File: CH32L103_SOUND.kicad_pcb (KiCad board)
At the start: 2 copper layers, 38 x 19.6 mm, 47 parts, among them J1 USB_C_Receptacle_PowerOnly_6P, J2 Conn_01x04, J3 Conn_01x05, J4 Conn_01x02, Q1 AO3400A, U1 USBLC6-2SC6, U2 TP4057, U3 HT7533-1, U4 CS588, U5 CH32L103F8U6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

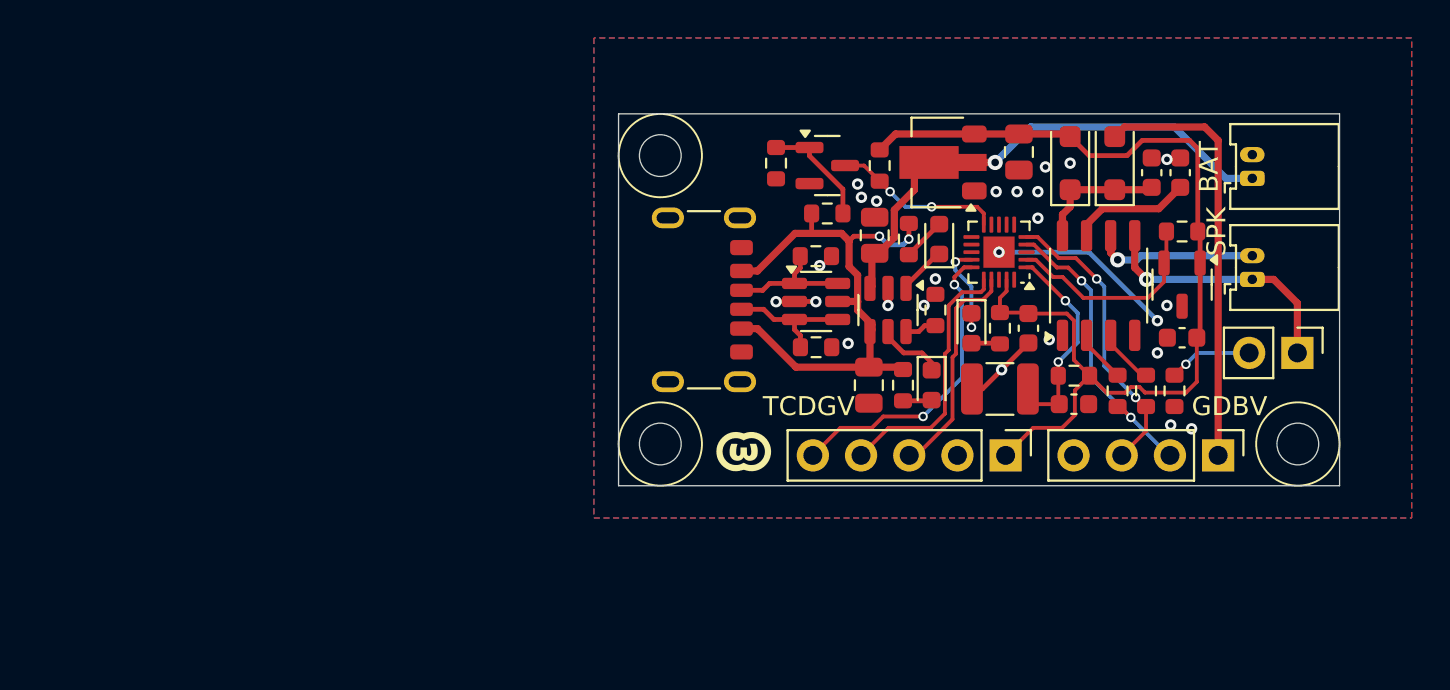
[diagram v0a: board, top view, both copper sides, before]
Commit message: 修改引脚布局
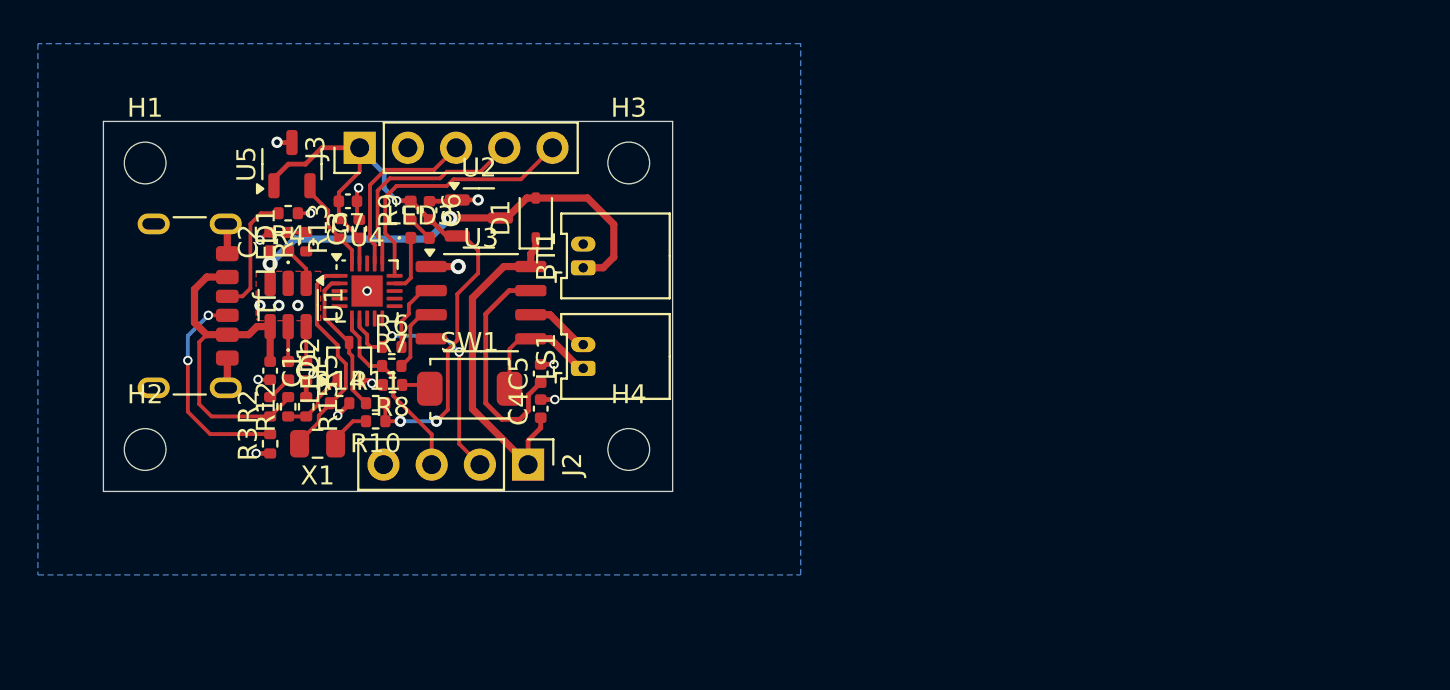
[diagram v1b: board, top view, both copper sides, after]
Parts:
- removed C8: 100NF, Capacitor_SMD:C_0603_1608Metric
- removed D2: K36, Diode_SMD:D_SOD-123F
- removed G***: LOGO, LOGO
- removed J4: Conn_01x02, Connector_PinHeader_2.54mm:PinHeader_1x02_P2.54mm_Vertical
- removed REF**: KiCad-Logo2_5mm_SilkScreen, Symbol:KiCad-Logo2_5mm_SilkScreen
- removed REF**: OSHW-Symbol_6.7x6mm_SilkScreen, Symbol:OSHW-Symbol_6.7x6mm_SilkScreen
- removed U6: CC6201, Package_TO_SOT_SMD:SOT-23-3
- added H4: MountingHole, MountingHole:MountingHole_2.2mm_M2_ISO14580, F.Cu at (83.4, 64.0)
- added R15: 10K, Resistor_SMD:R_0402_1005Metric, F.Cu at (66.4, 61.7)
- added SW1: SW_Push, Maiooo_Library:Button_2P, F.Cu at (75.0, 60.8)
- C1, C2, C3: footprint Capacitor_SMD:C_0805_2012Metric -> Capacitor_SMD:C_0402_1005Metric
- C4, C5, C6: footprint Capacitor_SMD:C_0603_1608Metric -> Capacitor_SMD:C_0402_1005Metric
- C7: value 50PF -> 100NF; footprint Capacitor_SMD:C_0603_1608Metric -> Capacitor_SMD:C_0402_1005Metric
- D1: value K36 -> 1N5819WS; footprint Diode_SMD:D_SOD-123F -> Diode_SMD:D_SOD-323
- LED1, LED2, LED3: footprint LED_SMD:LED_0603_1608Metric -> LED_SMD:LED_0402_1005Metric
- Q1: value AO3400A -> 2N7002W; footprint Package_TO_SOT_SMD:SOT-23 -> Package_TO_SOT_SMD:SOT-323_SC-70
- R1, R2, R3, R4, R5, R6, R7, R8, R9: footprint Resistor_SMD:R_0603_1608Metric -> Resistor_SMD:R_0402_1005Metric
- R10, R12: value 100K -> 1K; footprint Resistor_SMD:R_0603_1608Metric -> Resistor_SMD:R_0402_1005Metric
- R11: value 1K -> 1M; footprint Resistor_SMD:R_0603_1608Metric -> Resistor_SMD:R_0402_1005Metric
- R13: value 100K -> 1M; footprint Resistor_SMD:R_0603_1608Metric -> Resistor_SMD:R_0402_1005Metric
- R14: value 10K -> 1M; footprint Resistor_SMD:R_0603_1608Metric -> Resistor_SMD:R_0402_1005Metric
- U1: value USBLC6-2SC6 -> TP4057; footprint Package_TO_SOT_SMD:SOT-23-6 -> Package_TO_SOT_SMD:TSOT-23-6
- U2: value TP4057 -> HT7533-1; footprint Package_TO_SOT_SMD:TSOT-23-6 -> Maiooo_Library:HT7533s
- U3: value HT7533-1 -> CS588; footprint Package_TO_SOT_SMD:SOT-89-3 -> Package_SO:SOP-8_3.9x4.9mm_P1.27mm
- U4: value CS588 -> CH32L103F8U6; footprint Package_SO:SOP-8_3.9x4.9mm_P1.27mm -> Package_DFN_QFN:QFN-20-1EP_3x3mm_P0.4mm_EP1.65x1.65mm
- U5: value CH32L103F8U6 -> CC6201; footprint Package_DFN_QFN:QFN-20-1EP_3x3mm_P0.4mm_EP1.65x1.65mm -> Package_TO_SOT_SMD:SOT-23-3
- X1: value JYX-1210-C06 -> JYX-0805-C06; footprint Capacitor_SMD:C_1210_3225Metric -> Capacitor_SMD:C_0805_2012Metric
- moved R13 44.4 mm to (68.2, 52.4), turned to 90 degrees
- moved R12 41.4 mm to (65.5, 61.7), turned to 90 degrees
- moved R8 41.2 mm to (71.0, 60.6), turned to 180 degrees
- moved R7 39.8 mm to (70.9, 59.6), turned to 0 degrees
- moved C7 39.7 mm to (68.6, 50.9), turned to 180 degrees
- moved U4 38.6 mm to (69.6, 55.6), turned to 0 degrees
- moved R6 38.3 mm to (70.9, 58.6), turned to 0 degrees
- moved H3 38.2 mm to (83.4, 48.9)
- moved J3 37.7 mm to (69.3, 48.1), turned to 90 degrees
- moved U5 37.6 mm to (65.7, 49.0), turned to 90 degrees
- moved J2 36.4 mm to (78.1, 64.8)
- moved X1 36.1 mm to (67.0, 63.7)
- moved BT1 35.6 mm to (81.0, 54.4)
- moved LS1 35.6 mm to (81.0, 59.7)
- moved C5 35.3 mm to (78.8, 60.0)
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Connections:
- C4 pad 1: Net-(D1-K) -> Dl_POWER
- C5 pad 1: Net-(U4-VREF) -> Net-(U3-VREF)
- C7 pad 1: PA0 -> GND
- C7 pad 2: GND -> +3.3V
- D1 pad 1: Net-(D1-K) -> Dl_POWER
- D1 pad 2: +3.3V -> BAT
- LS1 pad 1: Net-(J4-Pin_1) -> Net-(U3-SPK1)
- LS1 pad 2: Net-(U4-SPK2) -> Net-(U3-SPK2)
- Q1 pad 3: PB11 -> PA1
- R10 pad 1: PB11 -> +3.3V
- R10 pad 2: +3.3V -> Net-(R10-Pad2)
- R11 pad 1: Net-(Q1-G) -> PA1
- R11 pad 2: VBUS -> +3.3V
- R12 pad 1: +3.3V -> Net-(Q1-G)
- R12 pad 2: PA0 -> VBUS
- R13 pad 1: PA1 -> PA6
- R14 pad 1: GND -> PA0
- R14 pad 2: Net-(Q1-G) -> GND
- R5 pad 1: Net-(U2-PROG) -> Net-(U1-PROG)
- R6 pad 2: Net-(U4-IO3) -> Net-(U3-IO3)
- R7 pad 2: Net-(U4-IO2) -> Net-(U3-IO2)
- U1 pad 1: /CC1 -> Net-(LED1-K)
- U1 pad 3: /CC2 -> BAT
- U1 pad 4: /CC2 -> VBUS
- U1 pad 5: VBUS -> Net-(LED2-K)
- U1 pad 6: /CC1 -> Net-(U1-PROG)
- U2 pad 1: Net-(LED1-K) -> GND
- U2 pad 2: GND -> BAT
- U2 pad 3: BAT -> +3.3V
- U3 pad 2: BAT -> Net-(U3-IO3)
- U3 pad 3: +3.3V -> Net-(U3-IO2)
- U4 pad 1: GND -> PA0
- U4 pad 2: Net-(U4-IO3) -> PA1
- U4 pad 3: Net-(U4-IO2) -> unconnected-(U4-PA2-Pad3)
- U4 pad 5: Net-(J4-Pin_1) -> unconnected-(U4-PA4-Pad5)
- U4 pad 6: Net-(U4-SPK2) -> ONE_Line
- U4 pad 7: Net-(U4-VREF) -> BUSY
- U4 pad 8: Net-(D1-K) -> unconnected-(U4-PB0-Pad8)
- U5 pad 1: PA0 -> +3.3V
- U5 pad 2: PA1 -> PA6
- U5 pad 3: unconnected-(U5-PA2-Pad3) -> GND
- X1 pad 1: PA0 -> Net-(R10-Pad2)
- X1 pad 2: GND -> PA0
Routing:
- net +3.3V: track 53.1 -> 35.1 mm, vias 0 -> 3
- net Net-(J4-Pin_1): track 13.6 -> 0.00 mm, vias 1 -> 0
- net Net-(U3-VREF): track 0.00 -> 12.1 mm
- net VBUS: track 29.8 -> 19.3 mm, vias 2 -> 0
- net PB11: track 8.95 -> 0.00 mm, vias 2 -> 0
- net Net-(U4-SPK2): track 8.61 -> 0.00 mm, vias 1 -> 0
- net Net-(D1-K): track 6.94 -> 0.00 mm
- net Net-(U3-SPK1): track 0.00 -> 6.84 mm
- net Net-(U4-VREF): track 6.42 -> 0.00 mm
- net ONE_Line: track 15.6 -> 9.82 mm, vias 2 -> 0
- net PA6: track 0.00 -> 5.02 mm
- net /CC2: track 6.88 -> 11.4 mm, vias 0 -> 2
- net Dl_POWER: track 22.6 -> 18.1 mm
- net Net-(U3-IO3): track 0.00 -> 3.88 mm
- net Net-(U3-IO2): track 0.00 -> 3.65 mm
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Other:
- board size 38 x 19.6 mm -> 30 x 19.5 mm
- board text removed: "BAT"
- board text removed: "GDBV"
- board text removed: "SPK"
- board text removed: "TCDGV"

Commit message: 修改错误丝印
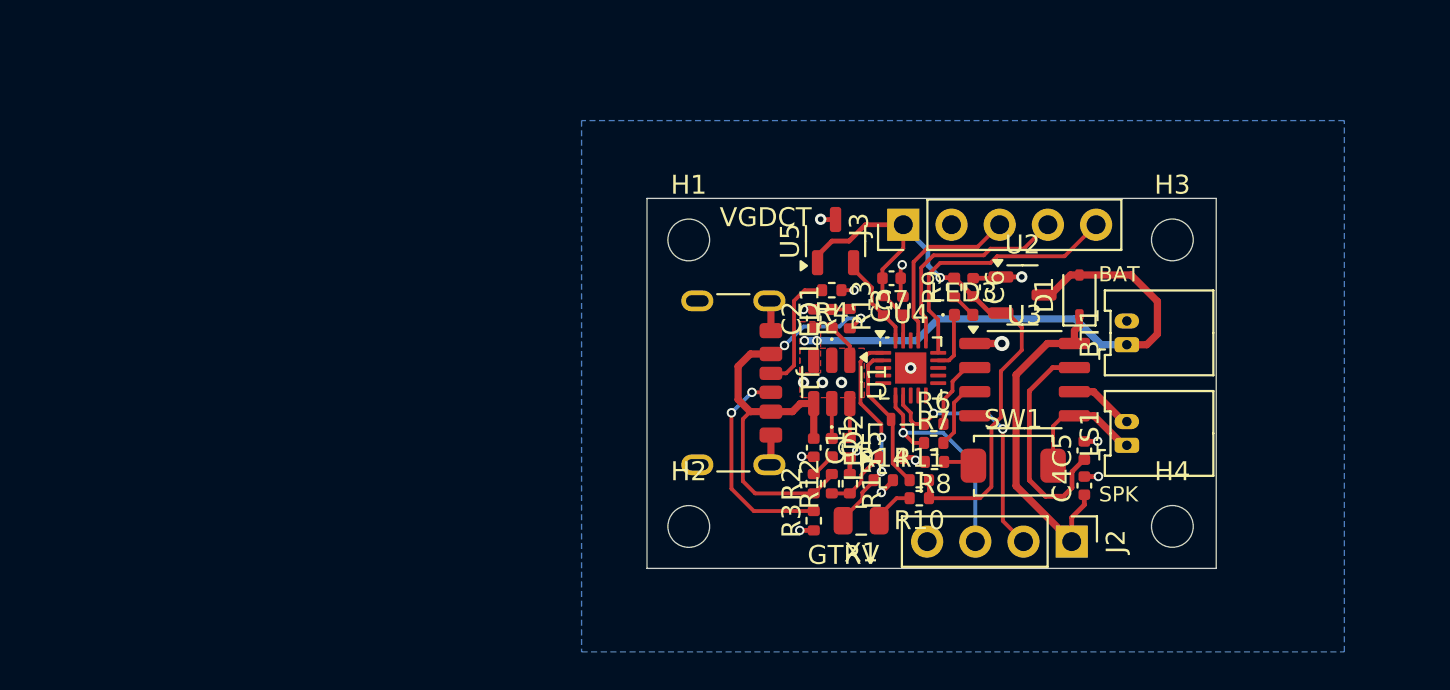
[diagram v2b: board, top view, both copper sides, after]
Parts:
- added G***: LOGO, LOGO, B.Cu at (96.3, 60.5)
- added REF**: WEEE-Logo_4.2x6mm_SilkScreen, Symbol:WEEE-Logo_4.2x6mm_SilkScreen, B.Cu at (104.2, 60.5)
- moved BT1 28.9 mm to (109.7, 58.5)
- moved C1 28.9 mm to (93.2, 63.9)
- moved C2 28.9 mm to (93.2, 57.1)
- moved C3 28.9 mm to (97.9, 56.4)
- moved C4 28.9 mm to (107.4, 65.9)
- moved C5 28.9 mm to (107.4, 64.0)
- moved C6 28.9 mm to (101.6, 55.4)
- moved D1 28.9 mm to (107.2, 55.8)
- moved H3 28.9 mm to (112.1, 52.9)
- moved H4 28.9 mm to (112.1, 68.0)
- moved J2 28.9 mm to (106.8, 68.8)
- moved J3 28.9 mm to (97.9, 52.1)
- moved LED1 28.9 mm to (94.1, 57.1)
- moved LED2 28.9 mm to (94.1, 63.9)
- moved LED3 28.9 mm to (101.1, 56.9)
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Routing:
- net VBUS: track 19.3 -> 25.6 mm, vias 0 -> 2
- net BAT: track 25.4 -> 28.6 mm
- net ONE_Line: track 9.82 -> 12.0 mm, vias 0 -> 1
- net PA0: track 11.4 -> 11.1 mm, vias 0 -> 2
- net +3.3V: vias 3 -> 1
- added copper zone on F.Cu, net BAT
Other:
- board text added: "@Maiooo"
- board text added: "BAT"
- board text added: "GTRV"
- board text added: "SOUND_HW V1.2.0 Ki"
- board text added: "SPK"
- board text added: "VGDCT"

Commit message: 新增注释
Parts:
- moved G*** 9.69 mm to (105.3, 64.3)
- moved REF** 2.87 mm to (105.3, 57.8)
